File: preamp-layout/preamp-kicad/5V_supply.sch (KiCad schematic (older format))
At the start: 0 parts

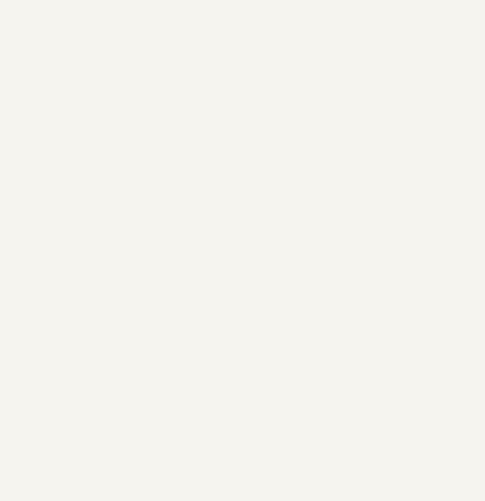
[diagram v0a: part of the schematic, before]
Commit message: BOM skeleton added. gitignore updated to ignore schematic bak files. General work done on the schematic layout.
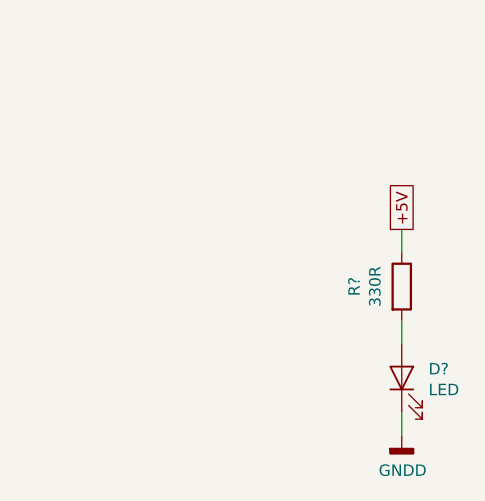
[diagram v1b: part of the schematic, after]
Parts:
- added D?: LED, symbol Device:LED
- added R?: 330R, symbol Device:R
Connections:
- new net: D?.2 (A), R?.2
- new net +5V: R?.1
- new net GNDD: D?.1 (K)
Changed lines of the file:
@@
 EESchema Schematic File Version 4
+LIBS:preamp-cache
 EELAYER 30 0
 EELAYER END
@@
 Text HLabel 2750 3650 0    50   UnSpc ~ 0
 AC_IN_-
+Text GLabel 9400 4200 1    50   UnSpc ~ 0
++5V
+$Comp
+L power:GNDD #PWR?
+U 1 1 5FFF96E2
+P 9400 5100
+F 0 "#PWR?" H 9400 4850 50  0001 C CNN
+F 1 "GNDD" H 9404 4945 50  0000 C CNN
+F 2 "" H 9400 5100 50  0001 C CNN
+F 3 "" H 9400 5100 50  0001 C CNN
+	1    9400 5100
+	1    0    0    -1
+$EndComp
+$Comp
+L Device:R R?
+U 1 1 5FFF96E8
+P 9400 4450
+AR Path="/5E2D8DA2/5FFF96E8" Ref="R?"  Part="1"
+AR Path="/5FFF96E8" Ref="R?"  Part="1"
+AR Path="/5E5EF2D4/5FFF96E8" Ref="R?"  Part="1"
+F 0 "R?" V 9193 4450 50  0000 C CNN
+F 1 "330R" V 9284 4450 50  0000 C CNN
+F 2 "" V 9330 4450 50  0001 C CNN
+F 3 "~" H 9400 4450 50  0001 C CNN
+	1    9400 4450
+	1    0    0    -1
+$EndComp
+$Comp
+L Device:LED D?
+U 1 1 5FFF96EE
+P 9400 4850
+AR Path="/5E2D8DA2/5FFF96EE" Ref="D?"  Part="1"
+AR Path="/5E5EF2D4/5FFF96EE" Ref="D?"  Part="1"
+F 0 "D?" V 9439 4733 50  0000 R CNN
+F 1 "LED" V 9348 4733 50  0000 R CNN
+F 2 "" H 9400 4850 50  0001 C CNN
+F 3 "~" H 9400 4850 50  0001 C CNN
+	1    9400 4850
+	0    -1   -1   0
+$EndComp
+Wire Wire Line
+	9400 4200 9400 4300
+Wire Wire Line
+	9400 4600 9400 4700
+Wire Wire Line
+	9400 5000 9400 5100
 $EndSCHEMATC

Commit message: readme references update. preamp-code updated to implement interrupts for encoder input. Layout general updates
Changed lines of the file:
@@
 $Descr A4 11693 8268
 encoding utf-8
-Sheet 7 8
+Sheet 6 11
 Title ""
 Date ""
@@
 $EndDescr
 Text HLabel 2750 3200 0    50   UnSpc ~ 0
-AC_IN_+
+AC+
 Text HLabel 2750 3650 0    50   UnSpc ~ 0
-AC_IN_-
+AC-
 Text GLabel 9400 4200 1    50   UnSpc ~ 0
 +5V
@@
 U 1 1 5FFF96E2
 P 9400 5100
+AR Path="/5E2D8DA2/5FFF96E2" Ref="#PWR?"  Part="1"
+AR Path="/5E5EF2D4/5FFF96E2" Ref="#PWR?"  Part="1"
 F 0 "#PWR?" H 9400 4850 50  0001 C CNN
 F 1 "GNDD" H 9404 4945 50  0000 C CNN

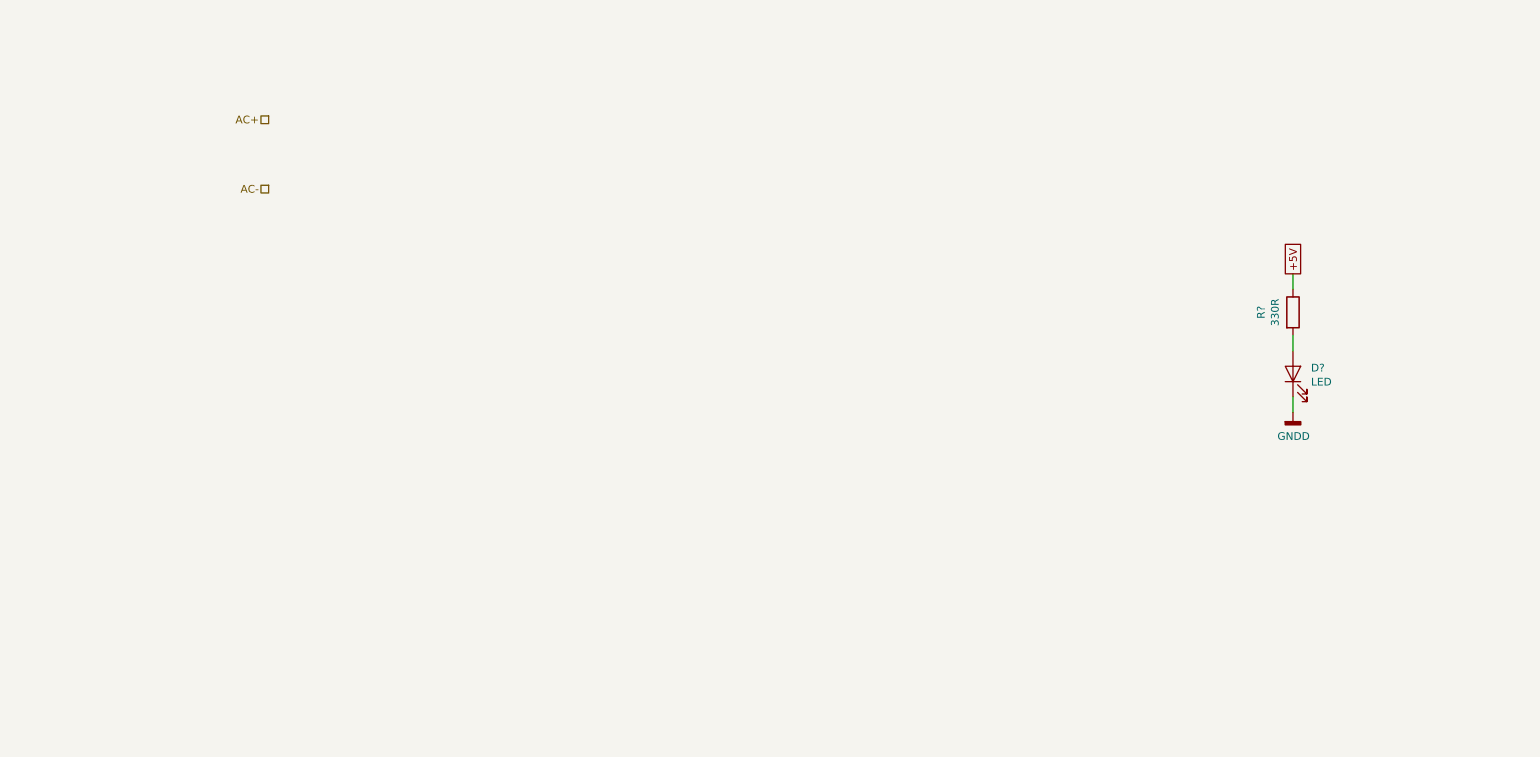
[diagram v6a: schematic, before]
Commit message: Updates
Minor Readme updates.
Schematic:
 - Bus connector lines replaced single wire connectors
 - Title block populated.
 - Power Supply updates.
 - Preliminary Front Panel.
 - Minor MCU work.
 -
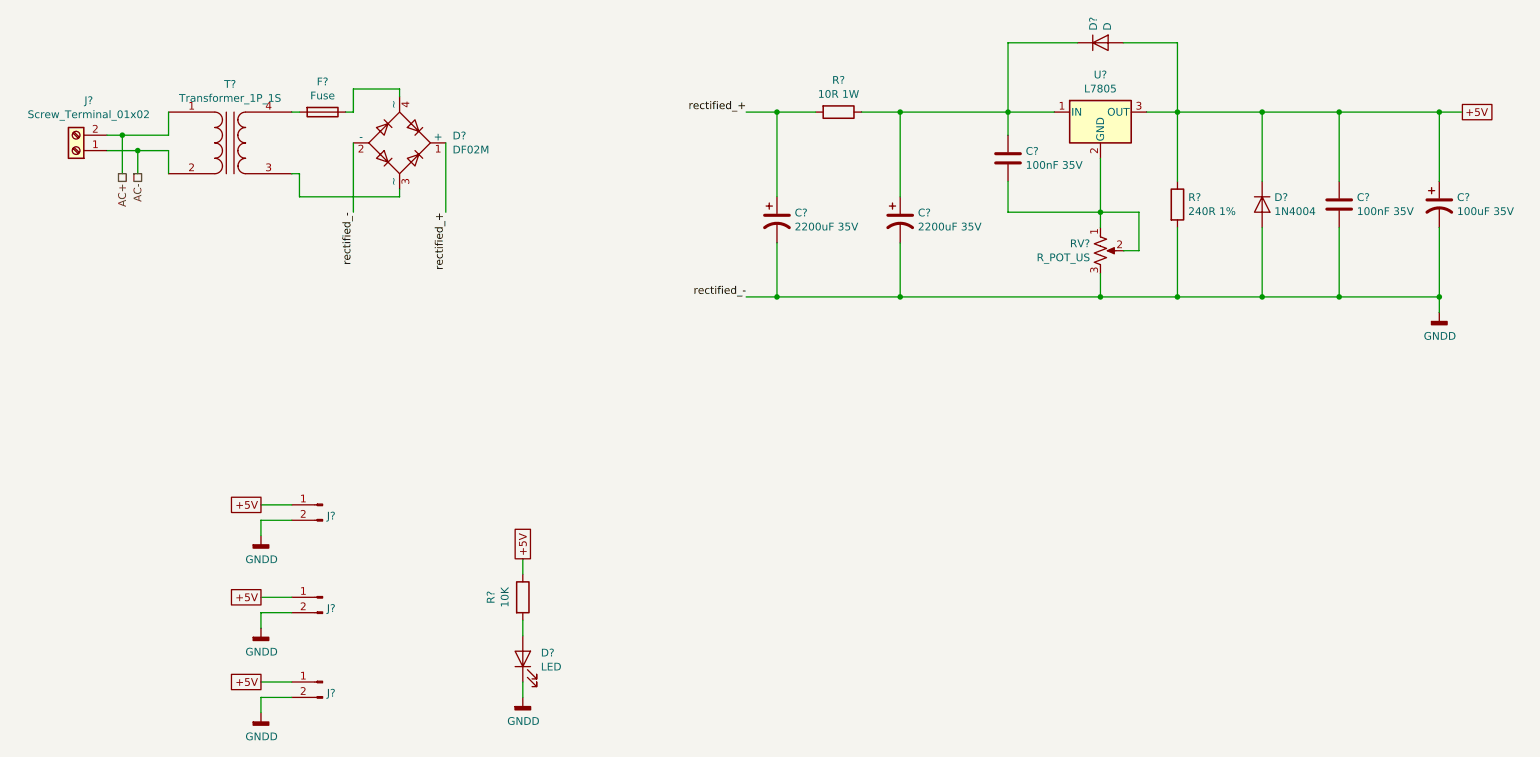
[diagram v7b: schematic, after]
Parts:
- removed D?: LED, symbol Device:LED
- removed R?: 330R, symbol Device:R
- added C? (x2): 100nF 35V, symbol Device:C
- added C? (x2): 2200uF 35V, symbol Device:CP1
- added C?: 100uF 35V, symbol Device:CP1
- added D?: 1N4004, symbol Device:D
- added D?: D, symbol Device:D
- added D?: LED, symbol Device:LED
- added D?: DF02M, Diode_THT:Diode_Bridge_DIP-4_W7.62mm_P5.08mm, symbol Diode_Bridge:DF02M
- added F?: Fuse, symbol Device:Fuse
- added J? (x3): Conn_01x02_Male, symbol Connector:Conn_01x02_Male
- added J?: Screw_Terminal_01x02, symbol Connector:Screw_Terminal_01x02
- added R?: 240R 1%, symbol Device:R
- added R?: 10R 1W, symbol Device:R
- added R?: 10K, symbol Device:R
- added RV?: R_POT_US, symbol Device:R_POT_US
- added T?: Transformer_1P_1S, symbol Device:Transformer_1P_1S
- added U?: L7805, symbol Regulator_Linear:L7805
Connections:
- net +5V: now also C?.1, C?.1, D?.1 (K), D?.2 (A), J?.1 (Pin_1), J?.1 (Pin_1), J?.1 (Pin_1), R?.1, R?.1, U?.3 (OUT)
- net AC+: now also J?.2 (Pin_2), T?.1 (AA)
- net AC-: now also J?.1 (Pin_1), T?.2 (AB)
- net GNDD: now also C?.2, C?.2, C?.2, C?.2, D?.1 (K), D?.2 (-), D?.2 (A), J?.2 (Pin_2), J?.2 (Pin_2), J?.2 (Pin_2), R?.2, RV?.3
- new net: C?.1, C?.1, D?.1 (K), R?.1, U?.1 (IN)
- new net: C?.2, RV?.1, RV?.2, U?.2 (GND)
- new net: D?.2 (A), R?.2
- new net: D?.4 (~~), F?.1
- new net: F?.2, T?.4 (SB)
- new net: D?.3 (~~), T?.3 (SA)
- new net rectified_+: C?.1, D?.1 (+), R?.2
